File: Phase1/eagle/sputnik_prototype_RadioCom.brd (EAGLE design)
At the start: 100 x 80 mm, 56 parts, among them Y1 32MHz

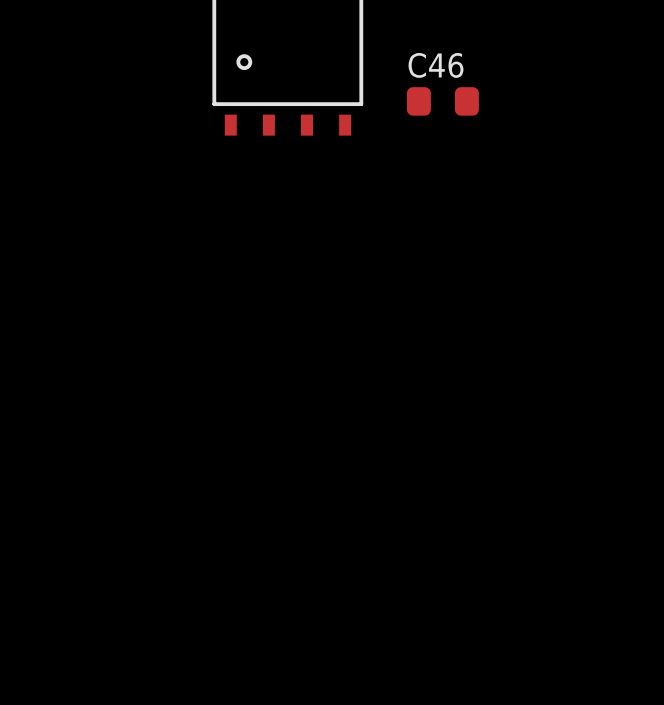
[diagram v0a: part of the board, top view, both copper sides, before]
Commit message: Added LNA LDO footprint and circuitry
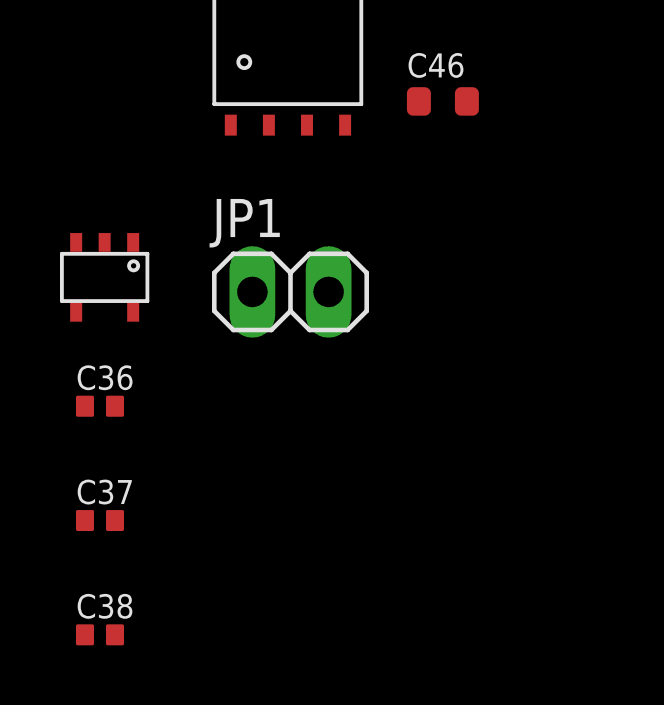
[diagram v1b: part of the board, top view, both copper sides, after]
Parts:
- added C36: 2.2uF, rcl_custom:.0402-B-NOSILK
- added C37: 10nF, rcl_custom:.0402-B-NOSILK
- added C38: 1uF, rcl_custom:.0402-B-NOSILK
- added JP1: (no value), psas_c3_team05:1X02
- added U$7: AAT3215, psas_c3_team05:AAT3215
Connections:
- new net N$1: C37.1, U$7.4
- new net N$9: C36.1, U$7.5
- new net VPA: C15.2, C16.2, C17.2, C18.2, C19.2, C20.2, C21.2, C22.2, C46.2, U$6.10, U$6.11, U$6.12, U$6.4, U$9.1, U$9.2
- net GND: now also C36.2, C37.2, C38.2, JP1.2, U$7.2
- net V+: now also C38.1, JP1.1, U$7.1; no longer C15.2, C16.2, C17.2, C18.2, C19.2, C20.2, C21.2, C22.2, C46.2, U$6.10, U$6.11, U$6.12, U$6.4, U$9.1, U$9.2
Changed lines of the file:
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@@
 <layer number="56" name="wert" color="7" fill="1" visible="no" active="no"/>
 <layer number="57" name="tCAD" color="7" fill="1" visible="no" active="no"/>
+<layer number="59" name="Invisible" color="7" fill="1" visible="no" active="no"/>
+<layer number="61" name="stand" color="7" fill="1" visible="no" active="no"/>
 <layer number="90" name="Modules" color="5" fill="1" visible="no" active="no"/>
 <layer number="91" name="Nets" color="2" fill="1" visible="no" active="no"/>
@@
 <layer number="127" name="_tValues" color="7" fill="1" visible="yes" active="yes"/>
 <layer number="128" name="_bValues" color="7" fill="1" visible="yes" active="yes"/>
+<layer number="130" name="bLogo" color="7" fill="1" visible="yes" active="yes"/>
 <layer number="131" name="tAdjust" color="7" fill="1" visible="yes" active="yes"/>
 <layer number="132" name="bAdjust" color="7" fill="1" visible="yes" active="yes"/>
@@
 <layer number="223" name="223bmp" color="7" fill="1" visible="yes" active="yes"/>
 <layer number="224" name="224bmp" color="7" fill="1" visible="yes" active="yes"/>
+<layer number="225" name="225bmp" color="7" fill="1" visible="yes" active="yes"/>
+<layer number="226" name="226bmp" color="7" fill="1" visible="yes" active="yes"/>
+<layer number="227" name="227bmp" color="7" fill="1" visible="yes" active="yes"/>
+<layer number="228" name="228bmp" color="7" fill="1" visible="yes" active="yes"/>
 <layer number="231" name="Eagle3D_PG1" color="7" fill="1" visible="yes" active="yes"/>
 <layer number="232" name="Eagle3D_PG2" color="7" fill="1" visible="yes" active="yes"/>
@@
 <element name="C46" library="rcl_custom" package=".0603-B-NOSILK" value="10uF" x="-60.96" y="-160.02"/>
 <element name="U$3" library="psas_c3_team05" package="LE25FU406B" value="LE25FU406B" x="-68.58" y="-156.21"/>
+<element name="JP1" library="psas_c3_team05" package="1X02" value="" x="-66.04" y="-166.37"/>
+<element name="U$7" library="psas_c3_team05" package="AAT3215" value="AAT3215" x="-73.66" y="-165.1"/>
+<element name="C36" library="rcl_custom" package=".0402-B-NOSILK" value="2.2uF" x="-72.39" y="-170.18"/>
+<element name="C37" library="rcl_custom" package=".0402-B-NOSILK" value="10nF" x="-72.39" y="-173.99"/>
+<element name="C38" library="rcl_custom" package=".0402-B-NOSILK" value="1uF" x="-72.39" y="-177.8"/>
 </elements>
 <signals>
@@
 <contactref element="C13" pad="1"/>
 <contactref element="C46" pad="1"/>
+<contactref element="JP1" pad="2"/>
+<contactref element="U$7" pad="2"/>
+<contactref element="C38" pad="2"/>
+<contactref element="C36" pad="2"/>
+<contactref element="C37" pad="2"/>
+<wire x1="-71.89" y1="-173.99" x2="-71.89" y2="-177.8" width="0" layer="19" extent="1-1"/>
+<wire x1="-71.89" y1="-170.18" x2="-71.89" y2="-173.99" width="0" layer="19" extent="1-1"/>
+<wire x1="-72.235" y1="-164.72" x2="-71.89" y2="-170.18" width="0" layer="19" extent="1-1"/>
+<wire x1="-64.77" y1="-166.37" x2="-72.235" y2="-164.72" width="0" layer="19" extent="1-1"/>
+<wire x1="-61.76" y1="-160.02" x2="-64.77" y2="-166.37" width="0" layer="19" extent="1-1"/>
 <wire x1="-61.76" y1="-154.94" x2="-61.76" y2="-160.02" width="0" layer="19" extent="1-1"/>
 <wire x1="-60.03" y1="-151.502" x2="-61.76" y2="-154.94" width="0" layer="19" extent="1-1"/>
@@
 <signal name="V+">
 <contactref element="U$5" pad="10"/>
-<contactref element="U$6" pad="4"/>
-<contactref element="C15" pad="2"/>
-<contactref element="C16" pad="2"/>
-<contactref element="C18" pad="2"/>
-<contactref element="C17" pad="2"/>
-<contactref element="U$6" pad="10"/>
-<contactref element="C21" pad="2"/>
-<contactref element="C22" pad="2"/>
-<contactref element="U$6" pad="11"/>
-<contactref element="C20" pad="2"/>
-<contactref element="U$6" pad="12"/>
-<contactref element="C19" pad="2"/>
-<contactref element="U$9" pad="1"/>
-<contactref element="U$9" pad="2"/>
-<contactref element="C46" pad="2"/>
 <contactref element="U$9" pad="6"/>
 <contactref element="C13" pad="2"/>
 <contactref element="U$9" pad="5"/>
-<wire x1="-60.16" y1="-154.94" x2="-60.16" y2="-160.02" width="0" layer="19" extent="1-1"/>
-<wire x1="-60.98" y1="-151.502" x2="-60.16" y2="-154.94" width="0" layer="19" extent="1-1"/>
-<wire x1="-61.93" y1="-151.502" x2="-60.98" y2="-151.502" width="0" layer="19" extent="1-1"/>
-<wire x1="-61.93" y1="-148.775" x2="-61.93" y2="-151.502" width="0" layer="19" extent="1-1"/>
-<wire x1="-60.98" y1="-148.775" x2="-61.93" y2="-148.775" width="0" layer="19" extent="1-1"/>
-<wire x1="-33.2035" y1="13.6896" x2="-60.98" y2="-148.775" width="0" layer="19" extent="1-1"/>
-<wire x1="-33.2035" y1="21.1048" x2="-33.2035" y2="13.6896" width="0" layer="19" extent="1-1"/>
-<wire x1="-31.3675" y1="21.1048" x2="-33.2035" y2="21.1048" width="0" layer="19" extent="1-1"/>
-<wire x1="-29.5315" y1="21.1048" x2="-31.3675" y2="21.1048" width="0" layer="19" extent="1-1"/>
-<wire x1="-29.68" y1="44.45" x2="-29.5315" y2="21.1048" width="0" layer="19" extent="1-1"/>
-<wire x1="-33.49" y1="44.45" x2="-29.68" y2="44.45" width="0" layer="19" extent="1-1"/>
-<wire x1="-37.3" y1="44.45" x2="-33.49" y2="44.45" width="0" layer="19" extent="1-1"/>
-<wire x1="-41.11" y1="44.45" x2="-37.3" y2="44.45" width="0" layer="19" extent="1-1"/>
-<wire x1="-44.92" y1="44.45" x2="-41.11" y2="44.45" width="0" layer="19" extent="1-1"/>
-<wire x1="-48.73" y1="44.45" x2="-44.92" y2="44.45" width="0" layer="19" extent="1-1"/>
-<wire x1="-52.54" y1="44.45" x2="-48.73" y2="44.45" width="0" layer="19" extent="1-1"/>
-<wire x1="-14.44" y1="48.26" x2="-29.68" y2="44.45" width="0" layer="19" extent="1-1"/>
-<wire x1="-13.785" y1="41.89" x2="-14.44" y2="48.26" width="0" layer="19" extent="1-1"/>
+<contactref element="JP1" pad="1"/>
+<contactref element="C38" pad="1"/>
+<contactref element="U$7" pad="1"/>
+<wire x1="-67.31" y1="-166.37" x2="-72.89" y2="-177.8" width="0" layer="19" extent="1-1"/>
+<wire x1="-71.285" y1="-164.72" x2="-67.31" y2="-166.37" width="0" layer="19" extent="1-1"/>
+<wire x1="-60.16" y1="-154.94" x2="-67.31" y2="-166.37" width="0" layer="19" extent="1-1"/>
+<wire x1="-60.98" y1="-148.775" x2="-60.16" y2="-154.94" width="0" layer="19" extent="1-1"/>
+<wire x1="-61.93" y1="-148.775" x2="-60.98" y2="-148.775" width="0" layer="19" extent="1-1"/>
+<wire x1="-13.785" y1="41.89" x2="-60.98" y2="-148.775" width="0" layer="19" extent="1-1"/>
 </signal>
 <signal name="PTA3">
@@
 <wire x1="-56.65" y1="-115.57" x2="-56.65" y2="-135.89" width="0" layer="19" extent="1-1"/>
 </signal>
-<signal name="N$26">
-<contactref element="C24" pad="1"/>
-<contactref element="L8" pad="2"/>
-<contactref element="C43" pad="+"/>
-<contactref element="R1" pad="2"/>
-<wire x1="-57.65" y1="-119.38" x2="-55.84" y2="-129.54" width="0" layer="19" extent="1-1"/>
-<wire x1="-18.25" y1="52.07" x2="-57.65" y2="-119.38" width="0" layer="19" extent="1-1"/>
-<wire x1="-14.44" y1="52.07" x2="-18.25" y2="52.07" width="0" layer="19" extent="1-1"/>
-</signal>
 <signal name="PE3">
 <contactref element="J1" pad="10"/>
@@
 <wire x1="-22.88" y1="11.4978" x2="-40.64" y2="15.875" width="0" layer="19" extent="1-1"/>
 </signal>
+<signal name="VPA">
+<contactref element="U$9" pad="1"/>
+<contactref element="U$9" pad="2"/>
+<contactref element="C46" pad="2"/>
+<contactref element="C19" pad="2"/>
+<contactref element="U$6" pad="12"/>
+<contactref element="C20" pad="2"/>
+<contactref element="C21" pad="2"/>
+<contactref element="U$6" pad="11"/>
+<contactref element="C22" pad="2"/>
+<contactref element="C16" pad="2"/>
+<contactref element="C15" pad="2"/>
+<contactref element="U$6" pad="4"/>
+<contactref element="C18" pad="2"/>
+<contactref element="U$6" pad="10"/>
+<contactref element="C17" pad="2"/>
+<wire x1="-60.98" y1="-151.502" x2="-60.16" y2="-160.02" width="0" layer="19" extent="1-1"/>
+<wire x1="-61.93" y1="-151.502" x2="-60.98" y2="-151.502" width="0" layer="19" extent="1-1"/>
+<wire x1="-33.2035" y1="13.6896" x2="-60.98" y2="-151.502" width="0" layer="19" extent="1-1"/>
+<wire x1="-33.2035" y1="21.1048" x2="-33.2035" y2="13.6896" width="0" layer="19" extent="1-1"/>
+<wire x1="-31.3675" y1="21.1048" x2="-33.2035" y2="21.1048" width="0" layer="19" extent="1-1"/>
+<wire x1="-29.5315" y1="21.1048" x2="-31.3675" y2="21.1048" width="0" layer="19" extent="1-1"/>
+<wire x1="-29.68" y1="44.45" x2="-29.5315" y2="21.1048" width="0" layer="19" extent="1-1"/>
+<wire x1="-33.49" y1="44.45" x2="-29.68" y2="44.45" width="0" layer="19" extent="1-1"/>
+<wire x1="-37.3" y1="44.45" x2="-33.49" y2="44.45" width="0" layer="19" extent="1-1"/>
+<wire x1="-41.11" y1="44.45" x2="-37.3" y2="44.45" width="0" layer="19" extent="1-1"/>
+<wire x1="-44.92" y1="44.45" x2="-41.11" y2="44.45" width="0" layer="19" extent="1-1"/>
+<wire x1="-48.73" y1="44.45" x2="-44.92" y2="44.45" width="0" layer="19" extent="1-1"/>
+<wire x1="-52.54" y1="44.45" x2="-48.73" y2="44.45" width="0" layer="19" extent="1-1"/>
+<wire x1="-14.44" y1="48.26" x2="-29.68" y2="44.45" width="0" layer="19" extent="1-1"/>
+</signal>
+<signal name="N$1">
+<contactref element="U$7" pad="4"/>
+<contactref element="C37" pad="1"/>
+<wire x1="-73.185" y1="-167.05" x2="-72.89" y2="-173.99" width="0" layer="19" extent="1-1"/>
+</signal>
+<signal name="N$2">
+<contactref element="L8" pad="2"/>
+<contactref element="R1" pad="2"/>
+<contactref element="C24" pad="1"/>
+<contactref element="C43" pad="+"/>
+<wire x1="-57.65" y1="-119.38" x2="-55.84" y2="-129.54" width="0" layer="19" extent="1-1"/>
+<wire x1="-18.25" y1="52.07" x2="-57.65" y2="-119.38" width="0" layer="19" extent="1-1"/>
+<wire x1="-14.44" y1="52.07" x2="-18.25" y2="52.07" width="0" layer="19" extent="1-1"/>
+</signal>
+<signal name="N$9">
+<contactref element="U$7" pad="5"/>
+<contactref element="C36" pad="1"/>
+<wire x1="-71.285" y1="-167.05" x2="-72.89" y2="-170.18" width="0" layer="19" extent="1-1"/>
+</signal>
 </signals>

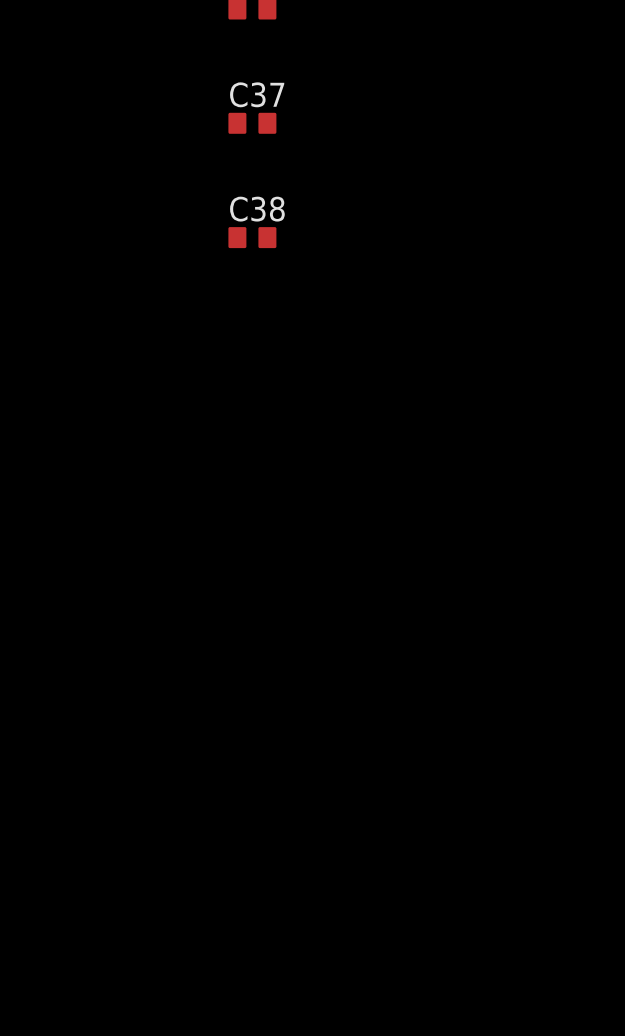
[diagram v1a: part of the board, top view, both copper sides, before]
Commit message: Added LDO for KW0x
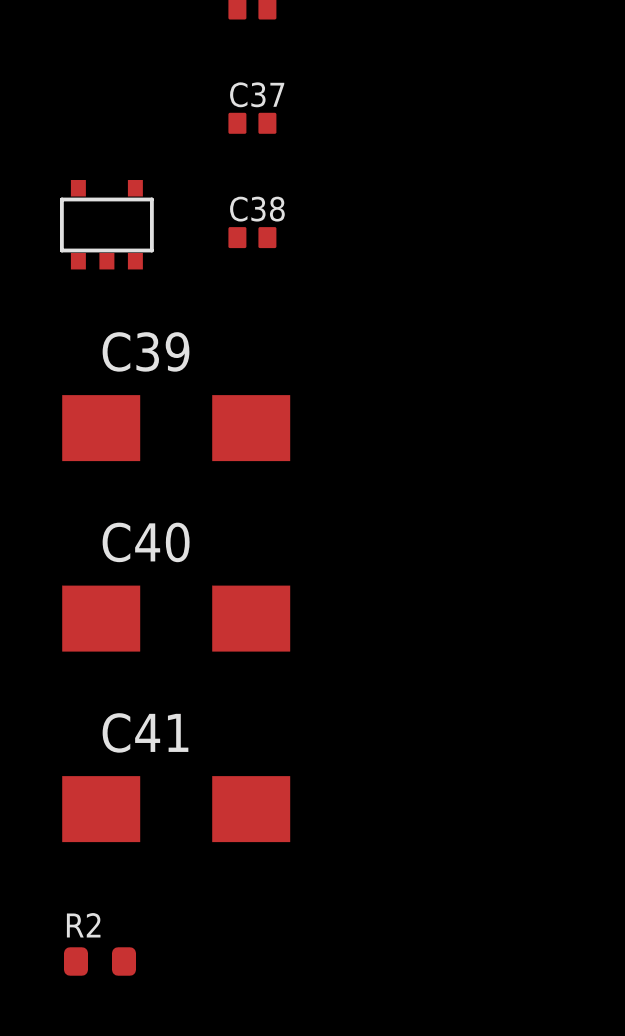
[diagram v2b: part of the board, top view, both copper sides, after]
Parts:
- added C39: 4.7uF, rcl:CT6032
- added C40: 1uF, rcl:CT6032
- added C41: .01uF, rcl:CT6032
- added R2: (no value), rcl_custom:.0603-B-NOSILK
- added U$8: TPS78930DBVT, psas_c3_team05:TPS78930DBVT
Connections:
- new net N$11: C41.+, U$8.4
- new net N$13: C39.-, R2.2
- new net N$3: C26.1, C27.1, C28.2, C29.2, C39.+, U$1.1, U$1.19, U$1.55, U$1.56, U$8.5
- net 3.3V: now also C40.+, U$3.8, U$8.1; no longer C26.1, C27.1, C28.2, C29.2, U$1.1, U$1.19, U$1.55, U$1.56
- net GND: now also C40.-, C41.-, R2.1, U$3.4, U$8.2, U$8.3
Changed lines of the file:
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@@
 <element name="C37" library="rcl_custom" package=".0402-B-NOSILK" value="10nF" x="-72.39" y="-173.99"/>
 <element name="C38" library="rcl_custom" package=".0402-B-NOSILK" value="1uF" x="-72.39" y="-177.8"/>
+<element name="U$8" library="psas_c3_team05" package="TPS78930DBVT" value="TPS78930DBVT" x="-78.74" y="-176.53"/>
+<element name="C39" library="rcl" package="CT6032" value="4.7uF" x="-74.93" y="-184.15"/>
+<element name="C40" library="rcl" package="CT6032" value="1uF" x="-74.93" y="-190.5"/>
+<element name="C41" library="rcl" package="CT6032" value=".01uF" x="-74.93" y="-196.85"/>
+<element name="R2" library="rcl_custom" package=".0603-B-NOSILK" value="" x="-77.47" y="-201.93"/>
 </elements>
 <signals>
@@
 <contactref element="C36" pad="2"/>
 <contactref element="C37" pad="2"/>
+<contactref element="U$3" pad="4"/>
+<contactref element="U$8" pad="2"/>
+<contactref element="U$8" pad="3"/>
+<contactref element="C41" pad="-"/>
+<contactref element="C40" pad="-"/>
+<contactref element="R2" pad="1"/>
 <wire x1="-71.89" y1="-173.99" x2="-71.89" y2="-177.8" width="0" layer="19" extent="1-1"/>
 <wire x1="-71.89" y1="-170.18" x2="-71.89" y2="-173.99" width="0" layer="19" extent="1-1"/>
+<wire x1="-76.29" y1="-178.587" x2="-71.89" y2="-177.8" width="0" layer="19" extent="1-1"/>
+<wire x1="-77.24" y1="-178.587" x2="-76.29" y2="-178.587" width="0" layer="19" extent="1-1"/>
 <wire x1="-72.235" y1="-164.72" x2="-71.89" y2="-170.18" width="0" layer="19" extent="1-1"/>
 <wire x1="-64.77" y1="-166.37" x2="-72.235" y2="-164.72" width="0" layer="19" extent="1-1"/>
-<wire x1="-61.76" y1="-160.02" x2="-64.77" y2="-166.37" width="0" layer="19" extent="1-1"/>
+<wire x1="-64.22" y1="-160.81" x2="-64.77" y2="-166.37" width="0" layer="19" extent="1-1"/>
+<wire x1="-61.76" y1="-160.02" x2="-64.22" y2="-160.81" width="0" layer="19" extent="1-1"/>
 <wire x1="-61.76" y1="-154.94" x2="-61.76" y2="-160.02" width="0" layer="19" extent="1-1"/>
 <wire x1="-60.03" y1="-151.502" x2="-61.76" y2="-154.94" width="0" layer="19" extent="1-1"/>
+<wire x1="-72.43" y1="-190.5" x2="-76.29" y2="-178.587" width="0" layer="19" extent="1-1"/>
+<wire x1="-72.43" y1="-196.85" x2="-72.43" y2="-190.5" width="0" layer="19" extent="1-1"/>
+<wire x1="-78.27" y1="-201.93" x2="-72.43" y2="-196.85" width="0" layer="19" extent="1-1"/>
 <wire x1="-50.84" y1="-129.54" x2="-60.03" y2="-151.502" width="0" layer="19" extent="1-1"/>
 <wire x1="-56.65" y1="-119.38" x2="-50.84" y2="-129.54" width="0" layer="19" extent="1-1"/>
@@
 </signal>
 <signal name="3.3V">
-<contactref element="C27" pad="1"/>
-<contactref element="U$1" pad="56"/>
-<contactref element="C29" pad="2"/>
-<contactref element="U$1" pad="1"/>
-<contactref element="U$1" pad="55"/>
-<contactref element="C26" pad="1"/>
-<contactref element="U$1" pad="19"/>
-<contactref element="C28" pad="2"/>
 <contactref element="C30" pad="2"/>
 <contactref element="U$1" pad="43"/>
@@
 <contactref element="C31" pad="2"/>
 <contactref element="J1" pad="1"/>
+<contactref element="U$3" pad="8"/>
+<contactref element="C40" pad="+"/>
+<contactref element="U$8" pad="1"/>
+<wire x1="-78.19" y1="-178.587" x2="-68.03" y2="-155.51" width="0" layer="19" extent="1-1"/>
+<wire x1="-77.43" y1="-190.5" x2="-78.19" y2="-178.587" width="0" layer="19" extent="1-1"/>
+<wire x1="-28.0078" y1="10.87" x2="-68.03" y2="-155.51" width="0" layer="19" extent="1-1"/>
+<wire x1="-23.88" y1="11.4978" x2="-28.0078" y2="10.87" width="0" layer="19" extent="1-1"/>
+<wire x1="-45.72" y1="14.605" x2="-28.0078" y2="10.87" width="0" layer="19" extent="1-1"/>
 <wire x1="-47.46" y1="31.75" x2="-45.72" y2="14.605" width="0" layer="19" extent="1-1"/>
 <wire x1="-52.54" y1="31.75" x2="-47.46" y2="31.75" width="0" layer="19" extent="1-1"/>
-<wire x1="-42.38" y1="31.75" x2="-47.46" y2="31.75" width="0" layer="19" extent="1-1"/>
-<wire x1="-37.3" y1="31.75" x2="-42.38" y2="31.75" width="0" layer="19" extent="1-1"/>
-<wire x1="-33.82" y1="31.75" x2="-37.3" y2="31.75" width="0" layer="19" extent="1-1"/>
-<wire x1="-28.74" y1="31.75" x2="-33.82" y2="31.75" width="0" layer="19" extent="1-1"/>
-<wire x1="-28.0078" y1="10.87" x2="-45.72" y2="14.605" width="0" layer="19" extent="1-1"/>
-<wire x1="-23.88" y1="11.4978" x2="-28.0078" y2="10.87" width="0" layer="19" extent="1-1"/>
-<wire x1="-28.0078" y1="4.87" x2="-28.0078" y2="10.87" width="0" layer="19" extent="1-1"/>
-<wire x1="-28.0078" y1="4.37" x2="-28.0078" y2="4.87" width="0" layer="19" extent="1-1"/>
-<wire x1="-27.38" y1="3.7422" x2="-28.0078" y2="4.37" width="0" layer="19" extent="1-1"/>
-<wire x1="-20.2522" y1="6.37" x2="-23.88" y2="11.4978" width="0" layer="19" extent="1-1"/>
 </signal>
 <signal name="N$5">
@@
 <wire x1="-71.285" y1="-167.05" x2="-72.89" y2="-170.18" width="0" layer="19" extent="1-1"/>
 </signal>
+<signal name="N$3">
+<contactref element="U$1" pad="1"/>
+<contactref element="C27" pad="1"/>
+<contactref element="U$1" pad="19"/>
+<contactref element="U$1" pad="55"/>
+<contactref element="C29" pad="2"/>
+<contactref element="U$1" pad="56"/>
+<contactref element="C26" pad="1"/>
+<contactref element="C28" pad="2"/>
+<contactref element="U$8" pad="5"/>
+<contactref element="C39" pad="+"/>
+<wire x1="-77.43" y1="-184.15" x2="-78.19" y2="-176.155" width="0" layer="19" extent="1-1"/>
+<wire x1="-27.38" y1="3.7422" x2="-78.19" y2="-176.155" width="0" layer="19" extent="1-1"/>
+<wire x1="-28.0078" y1="4.37" x2="-27.38" y2="3.7422" width="0" layer="19" extent="1-1"/>
+<wire x1="-28.0078" y1="4.87" x2="-28.0078" y2="4.37" width="0" layer="19" extent="1-1"/>
+<wire x1="-20.2522" y1="6.37" x2="-27.38" y2="3.7422" width="0" layer="19" extent="1-1"/>
+<wire x1="-28.74" y1="31.75" x2="-20.2522" y2="6.37" width="0" layer="19" extent="1-1"/>
+<wire x1="-33.82" y1="31.75" x2="-28.74" y2="31.75" width="0" layer="19" extent="1-1"/>
+<wire x1="-37.3" y1="31.75" x2="-33.82" y2="31.75" width="0" layer="19" extent="1-1"/>
+<wire x1="-42.38" y1="31.75" x2="-37.3" y2="31.75" width="0" layer="19" extent="1-1"/>
+</signal>
+<signal name="N$11">
+<contactref element="U$8" pad="4"/>
+<contactref element="C41" pad="+"/>
+<wire x1="-77.43" y1="-196.85" x2="-76.29" y2="-176.155" width="0" layer="19" extent="1-1"/>
+</signal>
+<signal name="N$13">
+<contactref element="C39" pad="-"/>
+<contactref element="R2" pad="2"/>
+<wire x1="-72.43" y1="-184.15" x2="-76.67" y2="-201.93" width="0" layer="19" extent="1-1"/>
+</signal>
 </signals>
